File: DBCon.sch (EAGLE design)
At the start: 100 parts, among them M1 1_PIN, M10 1_PIN, M11 1_PIN, M12 1_PIN, M13 1_PIN, M14 1_PIN, M2 1_PIN, M3 1_PIN, M4 1_PIN, M5 1_PIN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

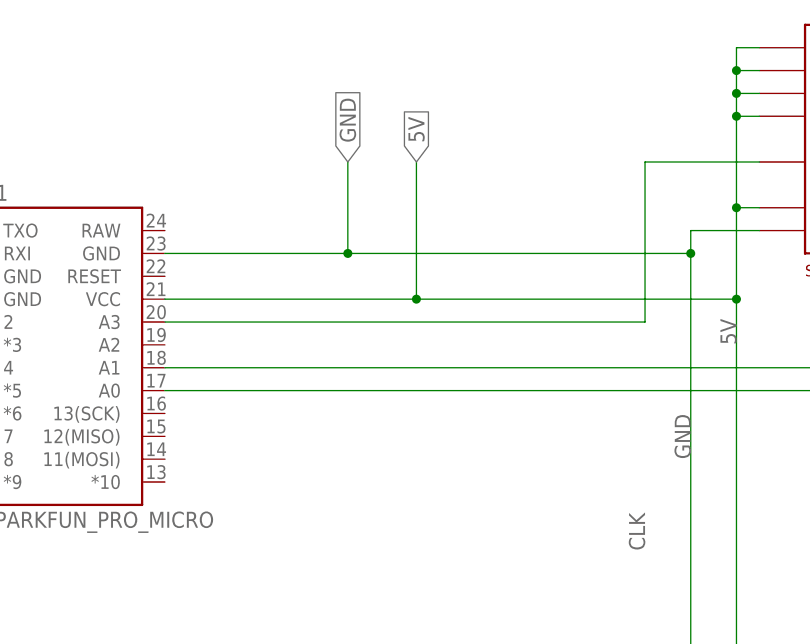
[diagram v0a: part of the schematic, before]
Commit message: Freed up analog pin
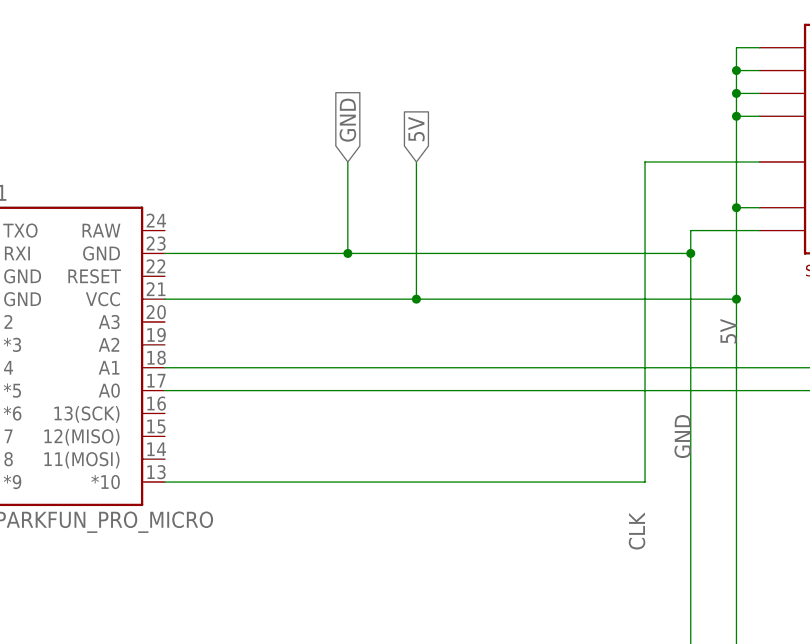
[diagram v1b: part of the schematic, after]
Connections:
- net CLK: now also B1.*10; no longer B1.A3
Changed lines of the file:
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@@
 <segment>
 <pinref part="SN74HC163D_1" gate="G$1" pin="CLK"/>
-<wire x1="22.86" y1="38.1" x2="22.86" y2="55.88" width="0.1524" layer="91"/>
 <wire x1="22.86" y1="55.88" x2="35.56" y2="55.88" width="0.1524" layer="91"/>
 <label x="22.86" y="12.7" size="1.778" layer="95" rot="R90"/>
-<pinref part="B1" gate="G$1" pin="A3"/>
-<wire x1="-30.48" y1="38.1" x2="22.86" y2="38.1" width="0.1524" layer="91"/>
+<pinref part="B1" gate="G$1" pin="*10"/>
+<wire x1="-30.48" y1="20.32" x2="22.86" y2="20.32" width="0.1524" layer="91"/>
+<wire x1="22.86" y1="20.32" x2="22.86" y2="55.88" width="0.1524" layer="91"/>
 </segment>
 </net>
